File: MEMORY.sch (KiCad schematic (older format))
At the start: 77 parts, among them U2 MCIMX7D7DVM10SC

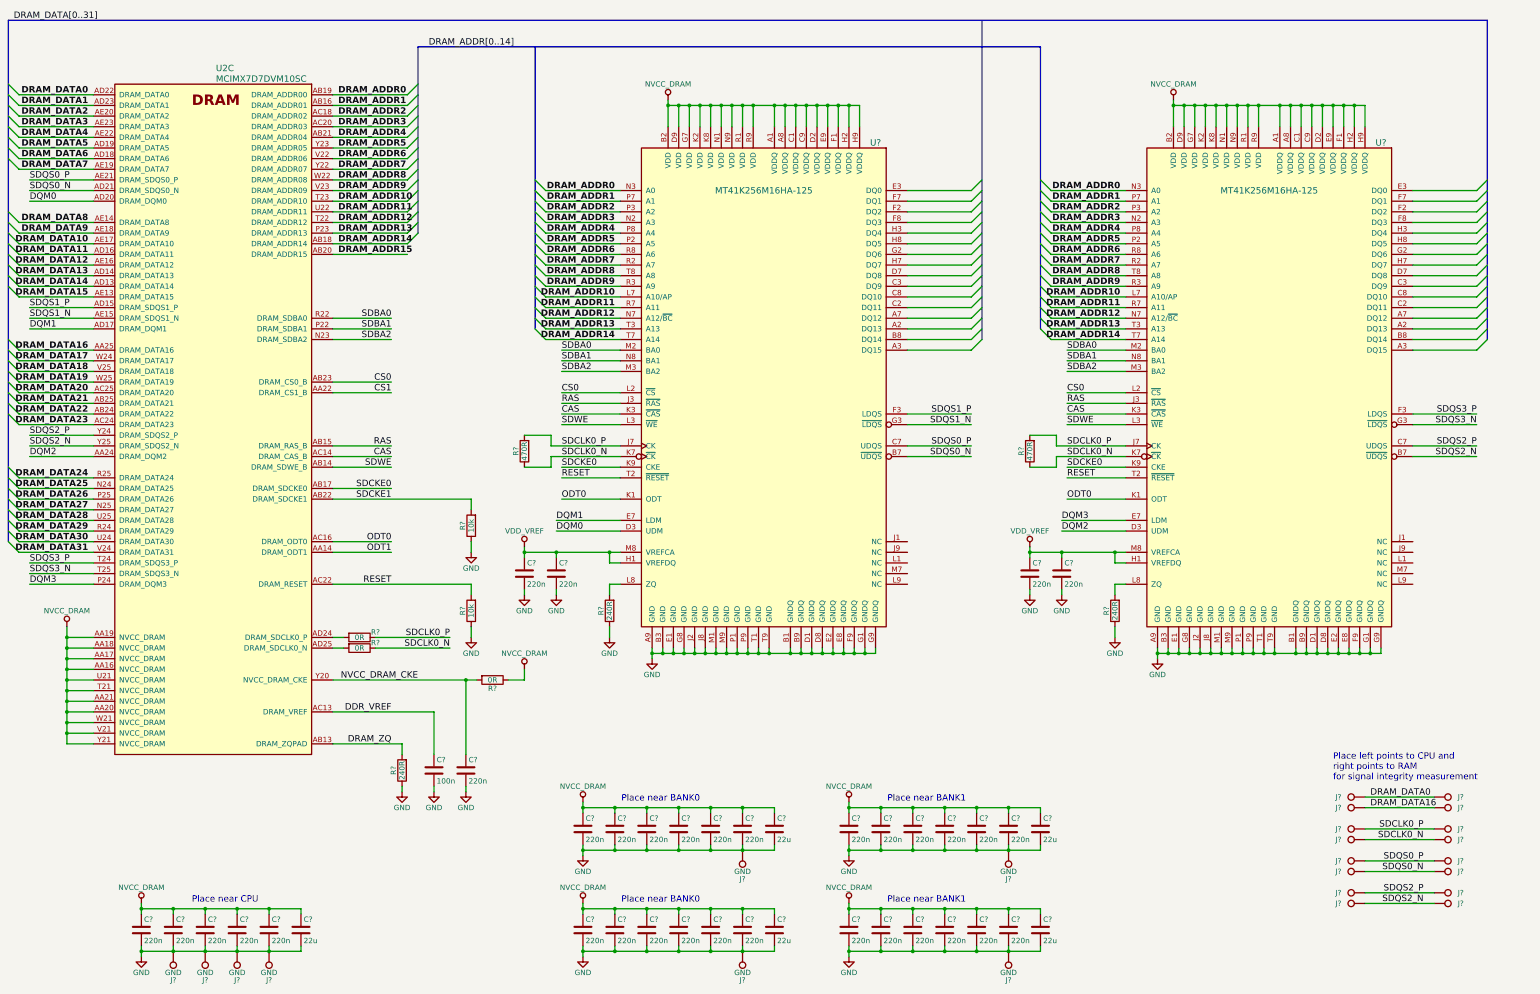
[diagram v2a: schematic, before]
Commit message: Prepare for two battery types NiMH battery for using the original battery pack LiPo battery for using long lasting modern battery
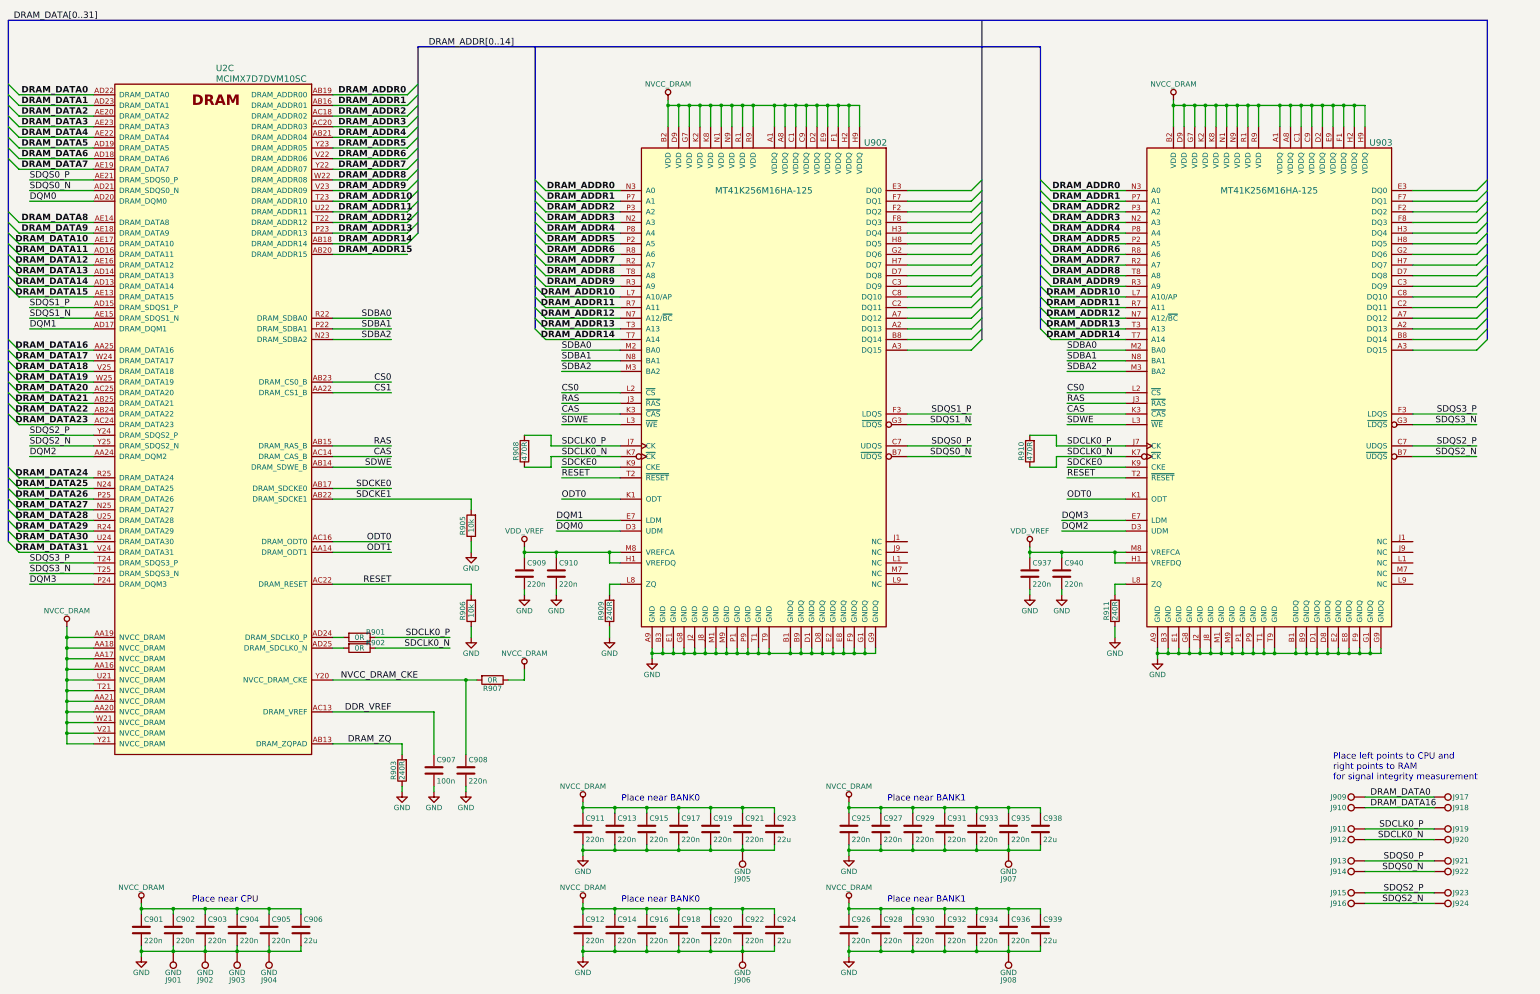
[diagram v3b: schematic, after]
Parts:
- gave numbers to parts that had none: 76

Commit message: Changed several voltage rail connections Removed non existing rails Added circuit for NiMH charging
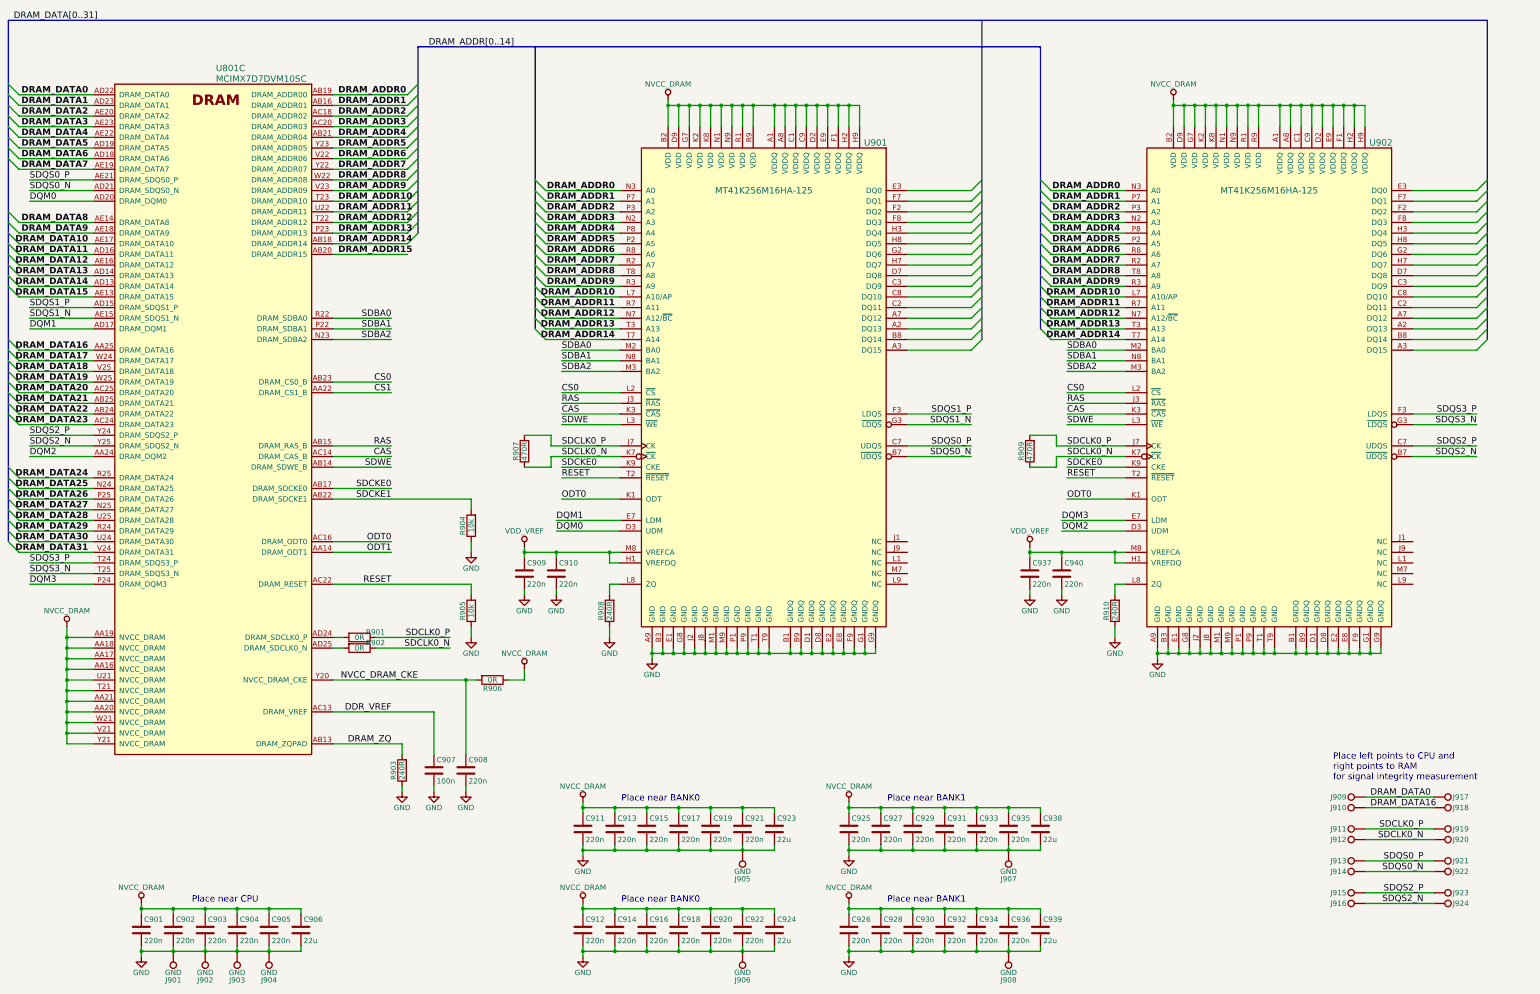
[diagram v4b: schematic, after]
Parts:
- renumbered R905 to R904, R906 to R905, R907 to R906, R908 to R907, R909 to R908, R910 to R909, R911 to R910, U2 to U801, U902 to U901, U903 to U902
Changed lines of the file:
@@
 $EndDescr
 $Comp
-L MCIMX7D7DVM10SC U2
+L MCIMX7D7DVM10SC U801
 U 3 1 5906320E
 P 3600 1550
-F 0 "U2" H 3600 1550 60  0000 L CNN
+F 0 "U801" H 3600 1550 60  0000 L CNN
 F 1 "MCIMX7D7DVM10SC" H 3600 1450 60  0000 L CNN
 F 2 "" H 1350 3250 60  0001 C CNN
@@
 $EndComp
 $Comp
-L MT41K256M16HA-125 U903
+L MT41K256M16HA-125 U902
 U 1 1 590B6323
 P 13500 2700
-F 0 "U903" H 14550 3150 60  0000 C CNN
+F 0 "U902" H 14550 3150 60  0000 C CNN
 F 1 "MT41K256M16HA-125" H 13500 2700 60  0000 C CNN
 F 2 "" H 13500 2700 60  0001 C CNN
@@
 DQM3
 $Comp
-L NVCC_DRAM #PWR901
+L NVCC_DRAM #PWR0165
 U 1 1 591D8B55
 P 2200 6800
-F 0 "#PWR901" H 2200 6650 50  0001 C CNN
+F 0 "#PWR0165" H 2200 6650 50  0001 C CNN
 F 1 "NVCC_DRAM" H 2200 6950 50  0000 C CNN
 F 2 "" H 2200 6800 50  0001 C CNN
@@
 Connection ~ 5950 7300
 $Comp
-L R R907
+L R R906
 U 1 1 591D9DF6
 P 6200 7300
-F 0 "R907" V 6280 7300 50  0000 C CNN
+F 0 "R906" V 6280 7300 50  0000 C CNN
 F 1 "0R" V 6200 7300 50  0000 C CNN
 F 2 "" V 6130 7300 50  0001 C CNN
@@
 	6500 7300 6500 7200
 $Comp
-L NVCC_DRAM #PWR911
+L NVCC_DRAM #PWR0166
 U 1 1 591D9FCD
 P 6500 7200
-F 0 "#PWR911" H 6500 7050 50  0001 C CNN
+F 0 "#PWR0166" H 6500 7050 50  0001 C CNN
 F 1 "NVCC_DRAM" H 6500 7350 50  0000 C CNN
 F 2 "" H 6500 7200 50  0001 C CNN
@@
 $EndComp
 $Comp
-L GND #PWR904
+L GND #PWR0167
 U 1 1 591DA1AD
 P 5350 8350
-F 0 "#PWR904" H 5350 8100 50  0001 C CNN
+F 0 "#PWR0167" H 5350 8100 50  0001 C CNN
 F 1 "GND" H 5350 8200 50  0000 C CNN
 F 2 "" H 5350 8350 50  0001 C CNN
@@
 $EndComp
 $Comp
-L GND #PWR905
+L GND #PWR0168
 U 1 1 591DA1D4
 P 5650 8350
-F 0 "#PWR905" H 5650 8100 50  0001 C CNN
+F 0 "#PWR0168" H 5650 8100 50  0001 C CNN
 F 1 "GND" H 5650 8200 50  0000 C CNN
 F 2 "" H 5650 8350 50  0001 C CNN
@@
 $EndComp
 $Comp
-L GND #PWR906
+L GND #PWR0169
 U 1 1 591DA1F4
 P 5950 8350
-F 0 "#PWR906" H 5950 8100 50  0001 C CNN
+F 0 "#PWR0169" H 5950 8100 50  0001 C CNN
 F 1 "GND" H 5950 8200 50  0000 C CNN
 F 2 "" H 5950 8350 50  0001 C CNN
@@
 DQM0
 $Comp
-L VDD_VREF #PWR909
+L VDD_VREF #PWR0170
 U 1 1 591DA9C3
 P 6500 6050
-F 0 "#PWR909" H 6500 5900 50  0001 C CNN
+F 0 "#PWR0170" H 6500 5900 50  0001 C CNN
 F 1 "VDD_VREF" H 6500 6200 50  0000 C CNN
 F 2 "" H 6500 6050 50  0001 C CNN
@@
 Connection ~ 7300 6100
 $Comp
-L GND #PWR910
+L GND #PWR0171
 U 1 1 591DAF04
 P 6500 6500
-F 0 "#PWR910" H 6500 6250 50  0001 C CNN
+F 0 "#PWR0171" H 6500 6250 50  0001 C CNN
 F 1 "GND" H 6500 6350 50  0000 C CNN
 F 2 "" H 6500 6500 50  0001 C CNN
@@
 	6500 6500 6500 6450
 $Comp
-L GND #PWR912
+L GND #PWR0172
 U 1 1 591DAF31
 P 6800 6500
-F 0 "#PWR912" H 6800 6250 50  0001 C CNN
+F 0 "#PWR0172" H 6800 6250 50  0001 C CNN
 F 1 "GND" H 6800 6350 50  0000 C CNN
 F 2 "" H 6800 6500 50  0001 C CNN
@@
 	6800 6500 6800 6450
 $Comp
-L GND #PWR917
+L GND #PWR0173
 U 1 1 591DB057
 P 7300 6900
-F 0 "#PWR917" H 7300 6650 50  0001 C CNN
+F 0 "#PWR0173" H 7300 6650 50  0001 C CNN
 F 1 "GND" H 7300 6750 50  0000 C CNN
 F 2 "" H 7300 6900 50  0001 C CNN
@@
 	7300 6800 7300 6900
 $Comp
-L R R909
+L R R908
 U 1 1 591DB05E
 P 7300 6650
-F 0 "R909" V 7380 6650 50  0000 C CNN
+F 0 "R908" V 7380 6650 50  0000 C CNN
 F 1 "240R" V 7300 6650 50  0000 C CNN
 F 2 "" V 7230 6650 50  0001 C CNN
@@
 	7300 6400 7300 6500
 $Comp
-L GND #PWR918
+L GND #PWR0174
 U 1 1 591DB3A1
 P 7700 7100
-F 0 "#PWR918" H 7700 6850 50  0001 C CNN
+F 0 "#PWR0174" H 7700 6850 50  0001 C CNN
 F 1 "GND" H 7700 6950 50  0000 C CNN
 F 2 "" H 7700 7100 50  0001 C CNN
@@
 SDQS2_N
 $Comp
-L GND #PWR927
+L GND #PWR0175
 U 1 1 591DD3B2
 P 12050 6900
-F 0 "#PWR927" H 12050 6650 50  0001 C CNN
+F 0 "#PWR0175" H 12050 6650 50  0001 C CNN
 F 1 "GND" H 12050 6750 50  0000 C CNN
 F 2 "" H 12050 6900 50  0001 C CNN
@@
 $EndComp
 $Comp
-L GND #PWR928
+L GND #PWR0176
 U 1 1 591DD3B8
 P 12450 7100
-F 0 "#PWR928" H 12450 6850 50  0001 C CNN
+F 0 "#PWR0176" H 12450 6850 50  0001 C CNN
 F 1 "GND" H 12450 6950 50  0000 C CNN
 F 2 "" H 12450 7100 50  0001 C CNN
@@
 	12050 6800 12050 6900
 $Comp
-L R R911
+L R R910
 U 1 1 591DD520
 P 12050 6650
-F 0 "R911" V 12130 6650 50  0000 C CNN
+F 0 "R910" V 12130 6650 50  0000 C CNN
 F 1 "240R" V 12050 6650 50  0000 C CNN
 F 2 "" V 11980 6650 50  0001 C CNN
@@
 	12050 6400 12050 6500
 $Comp
-L VDD_VREF #PWR924
+L VDD_VREF #PWR0177
 U 1 1 591DD5A2
 P 11250 6050
-F 0 "#PWR924" H 11250 5900 50  0001 C CNN
+F 0 "#PWR0177" H 11250 5900 50  0001 C CNN
 F 1 "VDD_VREF" H 11250 6200 50  0000 C CNN
 F 2 "" H 11250 6050 50  0001 C CNN
@@
 Connection ~ 11550 6100
 $Comp
-L GND #PWR925
+L GND #PWR0178
 U 1 1 591DD5B9
 P 11250 6500
-F 0 "#PWR925" H 11250 6250 50  0001 C CNN
+F 0 "#PWR0178" H 11250 6250 50  0001 C CNN
 F 1 "GND" H 11250 6350 50  0000 C CNN
 F 2 "" H 11250 6500 50  0001 C CNN
@@
 	11250 6500 11250 6450
 $Comp
-L GND #PWR926
+L GND #PWR0179
 U 1 1 591DD5C0
 P 11550 6500
-F 0 "#PWR926" H 11550 6250 50  0001 C CNN
+F 0 "#PWR0179" H 11550 6250 50  0001 C CNN
 F 1 "GND" H 11550 6350 50  0000 C CNN
 F 2 "" H 11550 6500 50  0001 C CNN
@@
 Connection ~ 8150 1900
 $Comp
-L NVCC_DRAM #PWR929
+L NVCC_DRAM #PWR0180
 U 1 1 591DF650
 P 12600 1850
-F 0 "#PWR929" H 12600 1700 50  0001 C CNN
+F 0 "#PWR0180" H 12600 1700 50  0001 C CNN
 F 1 "NVCC_DRAM" H 12600 2000 50  0000 C CNN
 F 2 "" H 12600 1850 50  0001 C CNN
@@
 	11500 5300 11500 5200
 $Comp
-L GND #PWR908
+L GND #PWR0181
 U 1 1 591E04B8
 P 6000 6900
-F 0 "#PWR908" H 6000 6650 50  0001 C CNN
+F 0 "#PWR0181" H 6000 6650 50  0001 C CNN
 F 1 "GND" H 6000 6750 50  0000 C CNN
 F 2 "" H 6000 6900 50  0001 C CNN
@@
 	6000 6800 6000 6900
 $Comp
-L R R906
+L R R905
 U 1 1 591E04BF
 P 6000 6650
-F 0 "R906" V 6080 6650 50  0000 C CNN
+F 0 "R905" V 6080 6650 50  0000 C CNN
 F 1 "10k" V 6000 6650 50  0000 C CNN
 F 2 "" V 5930 6650 50  0001 C CNN
@@
 	5100 6900 5800 6900
 $Comp
-L R R908
+L R R907
 U 1 1 591E22D7
 P 6500 5150
-F 0 "R908" V 6580 5150 50  0000 C CNN
+F 0 "R907" V 6580 5150 50  0000 C CNN
 F 1 "470R" V 6500 5150 50  0000 C CNN
 F 2 "" V 6430 5150 50  0001 C CNN
@@
 $EndComp
 $Comp
-L R R910
+L R R909
 U 1 1 591E263F
 P 11250 5150
-F 0 "R910" V 11330 5150 50  0000 C CNN
+F 0 "R909" V 11330 5150 50  0000 C CNN
 F 1 "470R" V 11250 5150 50  0000 C CNN
 F 2 "" V 11180 5150 50  0001 C CNN
@@
 $EndComp
 $Comp
-L GND #PWR907
+L GND #PWR0182
 U 1 1 591E355B
 P 6000 6100
-F 0 "#PWR907" H 6000 5850 50  0001 C CNN
+F 0 "#PWR0182" H 6000 5850 50  0001 C CNN
 F 1 "GND" H 6000 5950 50  0000 C CNN
 F 2 "" H 6000 6100 50  0001 C CNN
@@
 	6000 6000 6000 6100
 $Comp
-L R R905
+L R R904
 U 1 1 591E3562
 P 6000 5850
-F 0 "R905" V 6080 5850 50  0000 C CNN
+F 0 "R904" V 6080 5850 50  0000 C CNN
 F 1 "10k" V 6000 5850 50  0000 C CNN
 F 2 "" V 5930 5850 50  0001 C CNN
@@
 $EndComp
 $Comp
-L NVCC_DRAM #PWR902
+L NVCC_DRAM #PWR0183
 U 1 1 591E38C2
 P 2900 9400
-F 0 "#PWR902" H 2900 9250 50  0001 C CNN
+F 0 "#PWR0183" H 2900 9250 50  0001 C CNN
 F 1 "NVCC_DRAM" H 2900 9550 50  0000 C CNN
 F 2 "" H 2900 9400 50  0001 C CNN
@@
 	4400 9850 4400 9800
 $Comp
-L GND #PWR903
+L GND #PWR0184
 U 1 1 591E4185
 P 2900 9900
-F 0 "#PWR903" H 2900 9650 50  0001 C CNN
+F 0 "#PWR0184" H 2900 9650 50  0001 C CNN
 F 1 "GND" H 2900 9750 50  0000 C CNN
 F 2 "" H 2900 9900 50  0001 C CNN
@@
 $EndComp
 $Comp
-L NVCC_DRAM #PWR913
+L NVCC_DRAM #PWR0185
 U 1 1 591E46CB
 P 7050 8450
-F 0 "#PWR913" H 7050 8300 50  0001 C CNN
+F 0 "#PWR0185" H 7050 8300 50  0001 C CNN
 F 1 "NVCC_DRAM" H 7050 8600 50  0000 C CNN
 F 2 "" H 7050 8450 50  0001 C CNN
@@
 	8850 8900 8850 8850
 $Comp
-L GND #PWR914
+L GND #PWR0186
 U 1 1 591E46FE
 P 7050 8950
-F 0 "#PWR914" H 7050 8700 50  0001 C CNN
+F 0 "#PWR0186" H 7050 8700 50  0001 C CNN
 F 1 "GND" H 7050 8800 50  0000 C CNN
 F 2 "" H 7050 8950 50  0001 C CNN
@@
 $EndComp
 $Comp
-L NVCC_DRAM #PWR915
+L NVCC_DRAM #PWR0187
 U 1 1 591E4F77
 P 7050 9400
-F 0 "#PWR915" H 7050 9250 50  0001 C CNN
+F 0 "#PWR0187" H 7050 9250 50  0001 C CNN
 F 1 "NVCC_DRAM" H 7050 9550 50  0000 C CNN
 F 2 "" H 7050 9400 50  0001 C CNN
@@
 	8850 9850 8850 9800
 $Comp
-L GND #PWR916
+L GND #PWR0188
 U 1 1 591E4FAA
 P 7050 9900
-F 0 "#PWR916" H 7050 9650 50  0001 C CNN
+F 0 "#PWR0188" H 7050 9650 50  0001 C CNN
 F 1 "GND" H 7050 9750 50  0000 C CNN
 F 2 "" H 7050 9900 50  0001 C CNN
@@
 $EndComp
 $Comp
-L NVCC_DRAM #PWR920
+L NVCC_DRAM #PWR0189
 U 1 1 591E6BFA
 P 9550 8450
-F 0 "#PWR920" H 9550 8300 50  0001 C CNN
+F 0 "#PWR0189" H 9550 8300 50  0001 C CNN
 F 1 "NVCC_DRAM" H 9550 8600 50  0000 C CNN
 F 2 "" H 9550 8450 50  0001 C CNN
@@
 	11350 8900 11350 8850
 $Comp
-L GND #PWR921
+L GND #PWR0190
 U 1 1 591E6C39
 P 9550 8950
-F 0 "#PWR921" H 9550 8700 50  0001 C CNN
+F 0 "#PWR0190" H 9550 8700 50  0001 C CNN
 F 1 "GND" H 9550 8800 50  0000 C CNN
 F 2 "" H 9550 8950 50  0001 C CNN
@@
 $EndComp
 $Comp
-L NVCC_DRAM #PWR922
+L NVCC_DRAM #PWR0191
 U 1 1 591E6C59
 P 9550 9400
-F 0 "#PWR922" H 9550 9250 50  0001 C CNN
+F 0 "#PWR0191" H 9550 9250 50  0001 C CNN
 F 1 "NVCC_DRAM" H 9550 9550 50  0000 C CNN
 F 2 "" H 9550 9400 50  0001 C CNN
@@
 	11350 9850 11350 9800
 $Comp
-L GND #PWR923
+L GND #PWR0192
 U 1 1 591E6C98
 P 9550 9900
-F 0 "#PWR923" H 9550 9650 50  0001 C CNN
+F 0 "#PWR0192" H 9550 9650 50  0001 C CNN
 F 1 "GND" H 9550 9750 50  0000 C CNN
 F 2 "" H 9550 9900 50  0001 C CNN
@@
 	7850 1850 7850 2100
 $Comp
-L NVCC_DRAM #PWR919
+L NVCC_DRAM #PWR0193
 U 1 1 591DDA84
 P 7850 1850
-F 0 "#PWR919" H 7850 1700 50  0001 C CNN
+F 0 "#PWR0193" H 7850 1700 50  0001 C CNN
 F 1 "NVCC_DRAM" H 7850 2000 50  0000 C CNN
 F 2 "" H 7850 1850 50  0001 C CNN
@@
 $EndComp
 $Comp
-L MT41K256M16HA-125 U902
+L MT41K256M16HA-125 U901
 U 1 1 593FF3D0
 P 8750 2700
-F 0 "U902" H 9800 3150 60  0000 C CNN
+F 0 "U901" H 9800 3150 60  0000 C CNN
 F 1 "MT41K256M16HA-125" H 8750 2700 60  0000 C CNN
 F 2 "" H 8750 2700 60  0001 C CNN

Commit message: Created netlist with current components Foreward Annotation to Board
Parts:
- C901, C902, C903, C904, C905, C907, C908, C909, C910, C911, C912, C913, C914, C915, C916, C917, C918, C919, C920, C921, C922, C925, C926, C927, C928, C929, C930, C931, C932, C933, C934, C935, C936, C937, C940: footprint (none) -> Capacitors_SMD:C_0402
- C906, C923, C924, C938, C939: footprint (none) -> Capacitors_SMD:C_0603
- J901, J902, J903, J904, J905, J906, J907, J908, J909, J910, J911, J912, J913, J914, J915, J916, J917, J918, J919, J920, J921, J922, J923, J924: footprint (none) -> NokiaRetroFit:TP
- R901, R902, R903, R904, R905, R906, R907, R908, R909, R910: footprint (none) -> Resistors_SMD:R_0402
- U801: footprint (none) -> NokiaRetroFit:BGA_541_075_19x19
- U901, U902: footprint (none) -> NokiaRetroFit:MT41K256M16HA-125
